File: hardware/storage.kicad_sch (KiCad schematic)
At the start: 9 parts, among them J6 Micro_SD_Card_Det1, U21 EMMC5.1_BGA153

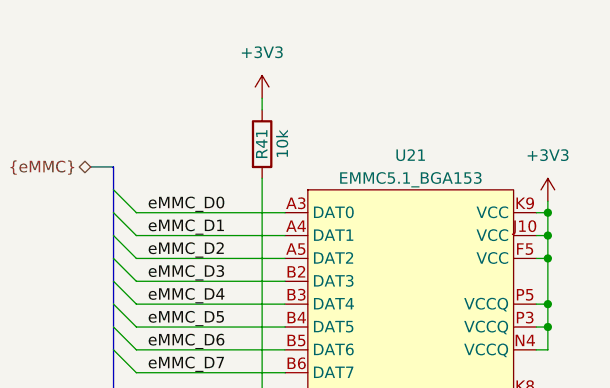
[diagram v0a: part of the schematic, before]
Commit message: Less than 100 traces left
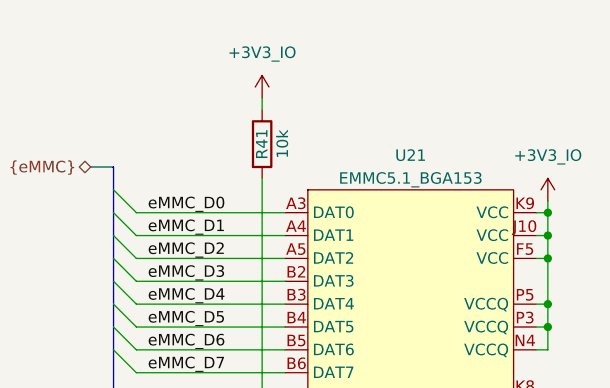
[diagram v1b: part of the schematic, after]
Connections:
- net +3V3 is gone; now on net +3V3_IO: R41.1, U21.C6 (VCCQ), U21.E6 (VCC), U21.F5 (VCC), U21.J10 (VCC), U21.K9 (VCC), U21.M4 (VCCQ), U21.N4 (VCCQ), U21.P3 (VCCQ), U21.P5 (VCCQ)
